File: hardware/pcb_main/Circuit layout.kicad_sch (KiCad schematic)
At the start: 117 parts, among them J1 FTSH-105-01-L-DV-K, U1 TPS7A2025PDQNR, U2 LM27761, U3 ADS1299IPAGR, U4 nRF52832-QFxx, Y1 32MHz

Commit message: Battery, zif added
nrf test points reduced
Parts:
- removed TP1: PWR, TestPoint:TestPoint_THTPad_2.5x2.5mm_Drill1.2mm, symbol Connector:TestPoint
- removed TP10: EEG2, TestPoint:TestPoint_THTPad_2.5x2.5mm_Drill1.2mm, symbol Connector:TestPoint
- removed TP11: EEG1, TestPoint:TestPoint_THTPad_2.5x2.5mm_Drill1.2mm, symbol Connector:TestPoint
- removed TP12: REF, TestPoint:TestPoint_THTPad_2.5x2.5mm_Drill1.2mm, symbol Connector:TestPoint
- removed TP13: BIAS, TestPoint:TestPoint_THTPad_2.5x2.5mm_Drill1.2mm, symbol Connector:TestPoint
- removed TP20: P21, TestPoint:TestPoint_THTPad_2.5x2.5mm_Drill1.2mm, symbol Connector:TestPoint
- removed TP23: P0, TestPoint:TestPoint_THTPad_2.5x2.5mm_Drill1.2mm, symbol Connector:TestPoint
- removed TP24: P1, TestPoint:TestPoint_THTPad_2.5x2.5mm_Drill1.2mm, symbol Connector:TestPoint
- removed TP25: P2, TestPoint:TestPoint_THTPad_2.5x2.5mm_Drill1.2mm, symbol Connector:TestPoint
- removed TP26: P3, TestPoint:TestPoint_THTPad_2.5x2.5mm_Drill1.2mm, symbol Connector:TestPoint
- removed TP27: DRDY_NRF, TestPoint:TestPoint_THTPad_2.5x2.5mm_Drill1.2mm, symbol Connector:TestPoint
- removed TP28: MISO_NRF, TestPoint:TestPoint_THTPad_2.5x2.5mm_Drill1.2mm, symbol Connector:TestPoint
- removed TP29: P6, TestPoint:TestPoint_THTPad_2.5x2.5mm_Drill1.2mm, symbol Connector:TestPoint
- removed TP30: CS_NRF, TestPoint:TestPoint_THTPad_2.5x2.5mm_Drill1.2mm, symbol Connector:TestPoint
- removed TP31: RESET_NRF, TestPoint:TestPoint_THTPad_2.5x2.5mm_Drill1.2mm, symbol Connector:TestPoint
- removed TP32: MOSI_NRF, TestPoint:TestPoint_THTPad_2.5x2.5mm_Drill1.2mm, symbol Connector:TestPoint
- removed TP33: P10, TestPoint:TestPoint_THTPad_2.5x2.5mm_Drill1.2mm, symbol Connector:TestPoint
- removed TP34: SCLK_NRF, TestPoint:TestPoint_THTPad_2.5x2.5mm_Drill1.2mm, symbol Connector:TestPoint
- removed TP35: P12, TestPoint:TestPoint_THTPad_2.5x2.5mm_Drill1.2mm, symbol Connector:TestPoint
- removed TP47: P25, TestPoint:TestPoint_THTPad_2.5x2.5mm_Drill1.2mm, symbol Connector:TestPoint
- removed TP48: P26, TestPoint:TestPoint_THTPad_2.5x2.5mm_Drill1.2mm, symbol Connector:TestPoint
- removed TP49: P27, TestPoint:TestPoint_THTPad_2.5x2.5mm_Drill1.2mm, symbol Connector:TestPoint
- removed TP50: P28, TestPoint:TestPoint_THTPad_2.5x2.5mm_Drill1.2mm, symbol Connector:TestPoint
- removed TP51: P29, TestPoint:TestPoint_THTPad_2.5x2.5mm_Drill1.2mm, symbol Connector:TestPoint
- removed TP52: P30, TestPoint:TestPoint_THTPad_2.5x2.5mm_Drill1.2mm, symbol Connector:TestPoint
- removed TP53: P31, TestPoint:TestPoint_THTPad_2.5x2.5mm_Drill1.2mm, symbol Connector:TestPoint
- removed TP8: EEG4, TestPoint:TestPoint_THTPad_2.5x2.5mm_Drill1.2mm, symbol Connector:TestPoint
- removed TP9: EEG3, TestPoint:TestPoint_THTPad_2.5x2.5mm_Drill1.2mm, symbol Connector:TestPoint
- added J2: 68710614522, foots:68710614522, symbol 68710614522:68710614522
- added U5: 1016TR, foots:1016TR, symbol 1016TR:1016TR
- TP14: value DRDY_ADS -> SPI_DRDY
- TP15: value MISO_ADS -> SPI_MISO
- TP16: value SCLK_ADS -> SPI_SCLK
- TP17: value CS_ADS -> SPI_CS
- TP18: value RESET_ADS -> RESET
- TP19: value MOSI_ADS -> SPI_MOSI
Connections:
- net +2V5: now also U3.1 (IN8N), U3.2 (IN8P), U3.3 (IN7N), U3.4 (IN7P), U3.5 (IN6N), U3.6 (IN6P), U3.7 (IN5N), U3.8 (IN5P)
- net +PWR: now also U5.1 (+)
- net GND: now also J2.7 (MP_1), J2.8 (MP_2), U5.2 (-); no longer J1.10
- net at R12.1: now also J2.6
- net at R9.1: now also J2.3
- net at R8.1: now also J2.2
- net at R11.2: now also J2.5
- net GPIO18: now reaches TP41.1, U4.21 (P0.18/SWO)
- net GPIO15: now reaches TP38.1, U4.18 (P0.15)
- net GPIO13: now reaches TP36.1, U4.16 (P0.13)
- net GPIO14: now reaches TP37.1, U4.17 (P0.14)
- net GPIO16: now reaches TP39.1, U4.19 (P0.16)
- net GPIO17: now reaches TP40.1, U4.20 (P0.17)
- net GPIO19: now reaches TP42.1, U4.22 (P0.19)
- net GPIO20: now reaches TP43.1, U4.23 (P0.20)
- net SWRST: now reaches U4.24 (P0.21/~{RESET})
- net SWRST: now also J1.10
- net SWCLK: now reaches J1.4, U4.25 (SWDCLK)
- net SWDIO: now reaches J1.2, U4.26 (SWDIO)
- net GPIO22: now reaches TP44.1, U4.27 (P0.22)
- net GPIO23: now reaches TP45.1, U4.28 (P0.23)
- net GPIO24: now reaches TP46.1, U4.29 (P0.24)
- net EEGBIAS: now reaches R13.2
- net EEGBIAS: now also J2.1
- net at R10.1: now also J2.4
- net CS renamed SPI_CS
- net DIN renamed SPI_MOSI
- net DRDY renamed SPI_DRDY
- net SCLK renamed SPI_SCLK
- no-connect marks 18 -> 30
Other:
- note added: "1/2 AA battery"
- moved on the sheet: C1, C2, C3, C4, C5, C6, C7, J1, R1, R10, R11, R12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

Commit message: Bridges done, main layout done
layer pours done
CHanged zif connector to 8 wide to the bridge
Changed voltage levels
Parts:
- removed H1, H2, H3, H4: MountingHole_Pad, MountingHole:MountingHole_2.2mm_M2_Pad_Via, symbol Mechanical:MountingHole_Pad
- removed J2: 68710614522, foots:68710614522, symbol 68710614522:68710614522
- removed R3: 100K, Resistor_SMD:R_0402_1005Metric_Pad0.72x0.64mm_HandSolder, symbol Device:R
- removed TP14: SPI_DRDY, TestPoint:TestPoint_THTPad_2.5x2.5mm_Drill1.2mm, symbol Connector:TestPoint
- removed TP15: SPI_MISO, TestPoint:TestPoint_THTPad_2.5x2.5mm_Drill1.2mm, symbol Connector:TestPoint
- removed TP16: SPI_SCLK, TestPoint:TestPoint_THTPad_2.5x2.5mm_Drill1.2mm, symbol Connector:TestPoint
- removed TP17: SPI_CS, TestPoint:TestPoint_THTPad_2.5x2.5mm_Drill1.2mm, symbol Connector:TestPoint
- removed TP18: RESET, TestPoint:TestPoint_THTPad_2.5x2.5mm_Drill1.2mm, symbol Connector:TestPoint
- removed TP19: SPI_MOSI, TestPoint:TestPoint_THTPad_2.5x2.5mm_Drill1.2mm, symbol Connector:TestPoint
- removed TP36: P13, TestPoint:TestPoint_THTPad_2.5x2.5mm_Drill1.2mm, symbol Connector:TestPoint
- removed TP37: P14, TestPoint:TestPoint_THTPad_2.5x2.5mm_Drill1.2mm, symbol Connector:TestPoint
- removed TP38: P15, TestPoint:TestPoint_THTPad_2.5x2.5mm_Drill1.2mm, symbol Connector:TestPoint
- removed TP39: P16, TestPoint:TestPoint_THTPad_2.5x2.5mm_Drill1.2mm, symbol Connector:TestPoint
- removed TP40: P17, TestPoint:TestPoint_THTPad_2.5x2.5mm_Drill1.2mm, symbol Connector:TestPoint
- removed TP41: P18, TestPoint:TestPoint_THTPad_2.5x2.5mm_Drill1.2mm, symbol Connector:TestPoint
- removed TP42: P19, TestPoint:TestPoint_THTPad_2.5x2.5mm_Drill1.2mm, symbol Connector:TestPoint
- removed TP43: P20, TestPoint:TestPoint_THTPad_2.5x2.5mm_Drill1.2mm, symbol Connector:TestPoint
- removed TP44: P22, TestPoint:TestPoint_THTPad_2.5x2.5mm_Drill1.2mm, symbol Connector:TestPoint
- removed TP45: P23, TestPoint:TestPoint_THTPad_2.5x2.5mm_Drill1.2mm, symbol Connector:TestPoint
- removed TP46: P24, TestPoint:TestPoint_THTPad_2.5x2.5mm_Drill1.2mm, symbol Connector:TestPoint
- removed TP54: GND, TestPoint:TestPoint_THTPad_2.5x2.5mm_Drill1.2mm, symbol Connector:TestPoint
- removed U1: TPS7A2025PDQNR, foots:TPS7A2025PDQNR, symbol EEG components:TPS7A2025PDQNR
- added J1: 687108149022, foots:687108149022, symbol 687108149022:687108149022
- added J2: PH1-06-UA, foots:PH1-06-UA, symbol PH1-06-UA:PH1-06-UA
- added J4: PH1-12-UA, foots:PH1-12-UA, symbol PH1-12-UA:PH1-12-UA
- added U2: TPS7A2030PDQNR, foots:TPS7A2030PDQNR, symbol TPS7A2030PDQNR:TPS7A2030PDQNR
- R1: value 100K -> 6.34K; Distributor Link https://www.mouser.co.uk/ProductDetail/Bourns/CR0402-JW-104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 -> https://www.mouser.co.uk/ProductDetail/Bourns/CR0402-FX-634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; Manufacturer Part Number CR0402-JW-104GLF -> CR0402-FX-6341GLF
- R2: value 5K -> 10K; Distributor Link https://www.mouser.co.uk/ProductDetail/YAGEO/RC0402FR-075KL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 -> https://www.mouser.co.uk/ProductDetail/Wurth-Elektronik/560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; Manufacturer YAGEO -> Wurth Elektronik; Manufacturer Part Number RC0402FR-075KL -> 560112110006
- TP1: renamed from TP2; value 2.5V -> 3V; footprint TestPoint:TestPoint_THTPad_2.5x2.5mm_Drill1.2mm -> TestPoint:TestPoint_Pad_D3.0mm
- TP2: renamed from TP3; value 2.5V -> -2V; footprint TestPoint:TestPoint_THTPad_2.5x2.5mm_Drill1.2mm -> TestPoint:TestPoint_Pad_D3.0mm
- U1: renamed from U5; Distributor Link (none) -> https://www.mouser.co.uk/ProductDetail/Keystone-Electronics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; Manufacturer (none) -> Keystone Electronics; Manufacturer Part Number (none) -> 1016TR
- renumbered C14 to C10, C15 to C11, C16 to C12, C17 to C13, C18 to C14, C19 to C15, C20 to C16, C21 to C17, C22 to C18, C23 to C19, C24 to C20, C25 to C21, C26 to C22, C27 to C23, C28 to C24, C29 to C25, C30 to C26, C31 to C27, C32 to C28, C33 to C29, C34 to C30, C35 to C31, C36 to C32, C37 to C33, C38 to C34, C12 to C8, C13 to C9, J1 to J3, L4 to L3, L3 to L4, R15 to R10, R16 to R11, R17 to R12, R18 to R13, R19 to R14, R20 to R15, R21 to R16, R8 to R3, R9 to R4, R10 to R5, R11 to R6, R12 to R7, R13 to R8, R14 to R9, U2 to U3, U3 to U4, U4 to U5
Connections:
- net EEGBIASOUT is gone; now on net EEGBIAS: C17.2, R8.1, R9.1, U4.62 (BIASIN), U4.63 (BIASOUT)
- net +PWR: now also J3.1, U2.3 (EN), U2.4 (IN)
- net EEGBIAS: no longer R8.2
- net GND: now also R2.2, J4.12, U2.2 (GND), U2.5 (Thermal_Pad)
- net GPIO13: now also J4.1
- net GPIO14: now also J4.2
- net GPIO15: now also J4.3
- net GPIO16: now also J4.4
- net GPIO17: now also J4.5
- net GPIO18: now also J4.6
- net GPIO19: now also J4.7
- net GPIO20: now also J4.8
- net GPIO22: now also J4.9
- net GPIO23: now also J4.10
- net GPIO24: now also J4.11
- net RESET: now also J2.5
- net SPI_CS: now also J2.4
- net SPI_MOSI: now also J2.6
- net SPI_SCLK: now also J2.3
- net EEG4R: now reaches R3.1
- net EEG4R: now also J1.2
- net VFB: now reaches R1.2
- net VFB: now also R2.1, U3.5 (VFB); no longer R2.2
- net EEG3R: now reaches R4.1
- net EEG3R: now also J1.3
- net EEG1R: now reaches R6.2
- net EEG1R: now also J1.7
- net EEGREFR: now reaches R7.1
- net EEGREFR: now also J1.5
- net CPOUT: now reaches C5.1, U3.3 (CPOUT)
- net C+: now reaches C4.1, U3.8 (C+)
- net C-: now reaches C4.2, U3.7 (C-)
- net EEG2R: now reaches R5.1
- net EEG2R: now also J1.6
- net +2V5 renamed +3V
- net +3V: now also U2.1 (OUT); no longer J3.1
- net -2V5 renamed -2V
- net -2V: now also J1.1, J1.8, J1.MP1, J1.MP2
- net DOUT renamed SPI_MISO
- net SPI_MISO: now also J2.2
- net SPI_DRDY renamed DRDY
- net DRDY: now also J2.1
- new net EEGBIASR: J1.4, R8.2
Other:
- note added: "3.6V to -2V Inverter"
- note added: "3.6V to 3V Regulator"
- note removed: "3.7V to -2.5V Inverter"
- note removed: "3.7V to 2.5V Regulator"
- note removed: "Mounting Holes (M2)"
- company: (none) -> Author: Dillon Jayasinghe
- title: (none) ->  DAQ CIRCUIT
- moved on the sheet: C1, C10, C11, C12, C13, C14, C15, C16, C17, C18, C19, C2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

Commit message: both bridge finished
main pcb layout nearly there
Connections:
- net +3V: now also U4.10 (IN4P), U4.12 (IN3P), U4.14 (IN2P), U4.16 (IN1P)
- net -2V: now also J1.3, J1.6, U4.17 (SRB1); no longer J1.1, J1.8
- net EEG1R: now also J1.8; no longer J1.7
- net EEG2R: now also J1.5; no longer J1.6
- net EEG3R: now also J1.4; no longer J1.3
- net EEG4R: now also J1.1; no longer J1.2
- net EEGBIASR: now also J1.2; no longer J1.4
- net EEGREFR: now also J1.7; no longer J1.5
- net GND: now also U5.10 (P0.08), U5.11 (NFC1/P0.09), U5.12 (NFC2/P0.10), U5.14 (P0.11), U5.15 (P0.12), U5.2 (P0.00/XL1), U5.3 (P0.01/XL2), U5.32 (DEC2), U5.37 (P0.25), U5.38 (P0.26), U5.39 (P0.27), U5.4 (P0.02/AIN0), U5.40 (P0.28/AIN4), U5.41 (P0.29/AIN5), U5.42 (P0.30/AIN6), U5.43 (P0.31/AIN7), U5.5 (P0.03/AIN1), U5.6 (P0.04/AIN2), U5.7 (P0.05/AIN3), U5.8 (P0.06), U5.9 (P0.07)
- no-connect marks 30 -> 4
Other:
- moved on the sheet: C20, R5, R6

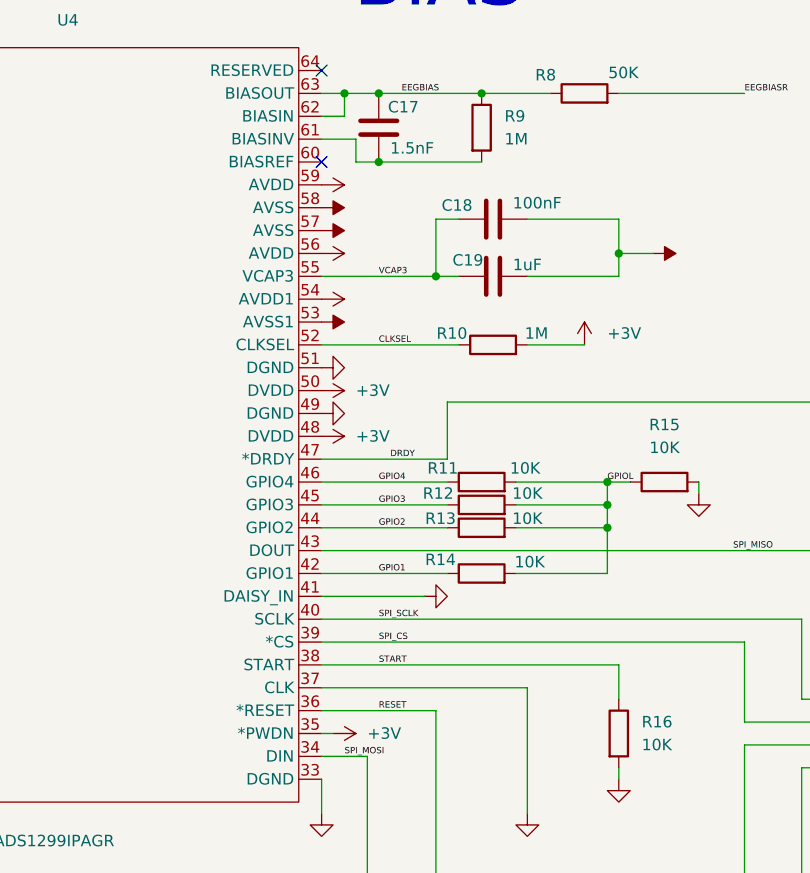
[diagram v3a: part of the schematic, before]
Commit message: layout finalised, routing started
more board fills, electrode routing done, faraday cage around electrode traces
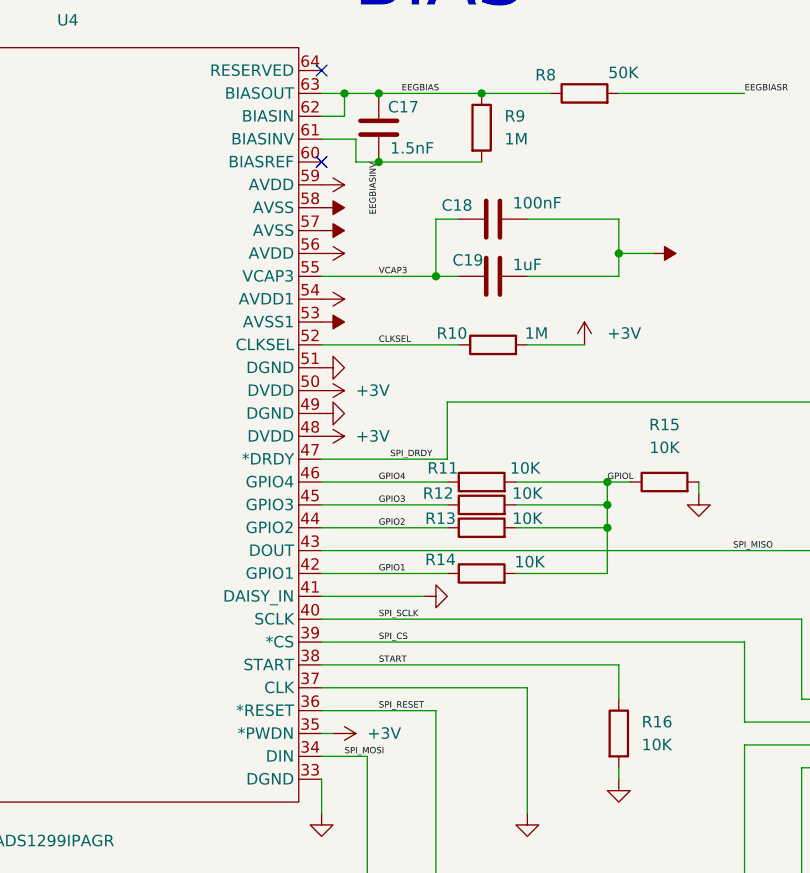
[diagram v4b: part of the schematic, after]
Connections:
- net EEGBIASINV: now reaches C17.1, R9.2, U4.61 (BIASINV)
- net DRDY renamed SPI_DRDY
- net RESET renamed SPI_RESET
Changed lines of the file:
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@@
 		)
 	)
-	(label "DRDY"
+	(label "SPI_DRDY"
 		(at 204.47 232.41 0)
 		(effects
@@
 		)
 	)
-	(label "RESET"
+	(label "SPI_RESET"
 		(at 203.2 260.35 0)
 		(effects
@@
 		)
 	)
+	(label "EEGBIASINV"
+		(at 203.2 199.39 270)
+		(effects
+			(font
+				(size 0.7 0.7)
+			)
+			(justify right bottom)
+		)
+	)

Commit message: Most of routing done
Just GNDing left
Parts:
- added C24: 4.7uF, Capacitor_SMD:C_0402_1005Metric_Pad0.74x0.62mm_HandSolder, symbol Device:C
- added D1: BAT30F4, foots:BAT30F4, symbol BAT30F4:BAT30F4
- TP1, TP2: footprint TestPoint:TestPoint_Pad_D3.0mm -> TestPoint:TestPoint_Pad_D2.0mm
- renumbered C24 to C25, C25 to C26, C26 to C27, C27 to C28, C28 to C29, C29 to C30, C30 to C31, C31 to C32, C32 to C33, C33 to C34, C34 to C35
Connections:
- net +3V: now also C24.2
- net +PWR: now also D1.1 (K); no longer U1.1 (+)
- net GND: now also C24.1
- new net PWR_D: D1.2 (A), U1.1 (+)
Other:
- moved on the sheet: U1

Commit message: All done, main and bridge 4 done
final push for a while
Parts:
- removed C6, C7: 1uF, Capacitor_SMD:C_0402_1005Metric_Pad0.74x0.62mm_HandSolder, symbol Device:C
- removed D1: BAT30F4, foots:BAT30F4, symbol BAT30F4:BAT30F4
- removed R1: 6.34K, Resistor_SMD:R_0402_1005Metric_Pad0.72x0.64mm_HandSolder, symbol Device:R
- removed R2: 10K, Resistor_SMD:R_0402_1005Metric_Pad0.72x0.64mm_HandSolder, symbol Device:R
- removed TP2: -2V, TestPoint:TestPoint_Pad_D2.0mm, symbol Connector:TestPoint
- removed U3: LM27761, foots:LM27761DSGT, symbol Regulator_SwitchedCapacitor:LM27761
- added L5: 2.2uH, foots:DFE252012F-2R2M=P2, symbol DFE252012F-2R2M=P2:DFE252012F-2R2M=P2
- added PS1: TPS613222ADBVT, foots:TPS613222ADBVT, symbol TPS613222ADBVT:TPS613222ADBVT
- added TP1: GND, TestPoint:TestPoint_Pad_D2.0mm, symbol Connector:TestPoint
- added TP3: 5V, TestPoint:TestPoint_Pad_D2.0mm, symbol Connector:TestPoint
- added U3: CDBU0130L, foots:CDBU0130L, symbol 2025-08-28_08-04-09:CDBU0130L
- C24, C3: Distributor Link https://www.mouser.co.uk/ProductDetail/KYOCERA-AVX/CM05X5R4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 -> https://www.digikey.co.uk/en/products/detail/kyocera-avx/KG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
- C4: value 1uF -> 33uF; footprint Capacitor_SMD:C_0402_1005Metric_Pad0.74x0.62mm_HandSolder -> Capacitor_SMD:C_0805_2012Metric; Distributor Link https://www.mouser.co.uk/ProductDetail/KYOCERA-AVX/04024D10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 -> https://www.digikey.co.uk/en/products/detail/tdk-corporatio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; Manufacturer KYOCERA AVX -> TDK Corporation; Manufacturer Part Number 04024D105KAT2A -> C2012X5R1A336M125AC
- C5: value 4.7uF -> 33uF; footprint Capacitor_SMD:C_0402_1005Metric_Pad0.74x0.62mm_HandSolder -> Capacitor_SMD:C_0805_2012Metric; Distributor Link https://www.mouser.co.uk/ProductDetail/KYOCERA-AVX/CM05X5R4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 -> https://www.digikey.co.uk/en/products/detail/tdk-corporatio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; Manufacturer KYOCERA AVX -> TDK Corporation; Manufacturer Part Number CM05X5R475M16AH -> C2012X5R1A336M125AC
- L4: Manufacturer Murata -> Murata Electronics
- renumbered TP1 to TP2
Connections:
- net -2V is gone; now on net GND: C12.2, C13.1, C14.2, C15.2, C16.2, C18.1, C19.2, C29.2, C30.2, C31.2, C32.2, C33.2, J1.3, J1.6, J1.MP1, J1.MP2, U4.17 (SRB1), U4.20 (AVSS), U4.23 (AVSS), U4.25 (VREFN), U4.32 (AVSS), U4.53 (AVSS1), U4.57 (AVSS), U4.58 (AVSS)
- net C- is gone; now on net GND: C4.2
- net CPOUT is gone; now on net +5V: C5.1
- net +3V: no longer C29.1, C30.1, C31.1, C32.1, C33.1, U4.1 (IN8N), U4.10 (IN4P), U4.12 (IN3P), U4.14 (IN2P), U4.16 (IN1P), U4.19 (AVDD), U4.2 (IN8P), U4.21 (AVDD), U4.22 (AVDD), U4.3 (IN7N), U4.4 (IN7P), U4.5 (IN6N), U4.54 (AVDD1), U4.56 (AVDD), U4.59 (AVDD), U4.6 (IN6P), U4.7 (IN5N), U4.8 (IN5P)
- net +PWR: now also L5.1, U3.1
- net GND: now also PS1.2 (GND), PS1.3 (NC_1), TP1.1; no longer L3.1 (FEED)
- net PWR_D: now also U3.2
- net RF_ANT: now also L3.1 (FEED); no longer L3.2 (NC)
- net C+ renamed +5V
- net +5V: now also C29.1, C30.1, C31.1, C32.1, C33.1, U4.1 (IN8N), U4.10 (IN4P), U4.12 (IN3P), U4.14 (IN2P), U4.16 (IN1P), U4.19 (AVDD), U4.2 (IN8P), U4.21 (AVDD), U4.22 (AVDD), U4.3 (IN7N), U4.4 (IN7P), U4.5 (IN6N), U4.54 (AVDD1), U4.56 (AVDD), U4.59 (AVDD), U4.6 (IN6P), U4.7 (IN5N), U4.8 (IN5P), PS1.4 (VOUT), PS1.5 (NC_2), TP3.1
- new net SW: L5.2, PS1.1 (SW)
- no-connect marks 4 -> 5
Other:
- note added: "3.6V to 5V Boost"
- note removed: "3.6V to -2V Inverter"
- moved on the sheet: C34, C35

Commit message: Final push for now
All bridges ordered, main DAQ ordered,
Main DAQ needed 1 tweak to prevent short circuit due to close by traces
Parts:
- renumbered C12 to C10, C13 to C11, C14 to C12, C15 to C13, C16 to C14, C17 to C15, C18 to C16, C19 to C17, C20 to C18, C21 to C19, C22 to C20, C23 to C21, C24 to C22, C25 to C23, C26 to C24, C27 to C25, C28 to C26, C29 to C27, C30 to C28, C31 to C29, C32 to C30, C33 to C31, C34 to C32, C35 to C33, C8 to C6, C9 to C7, C10 to C8, C11 to C9, U3 to D1, L5 to L1, L1 to L2, L2 to L3, L3 to L4, L4 to L5, PS1 to U3
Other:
- note added: "3.6V to 3V LDO"
- note added: "ADS1299 Decoupling"
- note added: "Analog"
- note added: "Digital"
- note removed: "3.6V to 3V Regulator"
- note removed: "A PWR"
- note removed: "ADS PWR"
- note removed: "D PWR"
- moved on the sheet: C1, C10, C11, C12, C13, C14, C15, C16, C17, C18, C19, C2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
